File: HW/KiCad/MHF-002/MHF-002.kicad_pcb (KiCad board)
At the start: 4 copper layers, 100 x 100 mm, 305 parts, among them J1 VGA, J10 I2C, J100 x, J101 x, J102 x, J103 x, J104 x, J105 x, J106 x, J107 +3V3, J108 GND, J109 +3V3, J11 + 5V -, J110 +5V, J111 GND, J112 GND, J113 SDCard, J114 VIN, J115 VI, J116 GND, J12 Reset, J13 +5V, J14 GND, J15 AREF, J16 XTAL2, J17 SDcard, J18 XTAL1, J19 AVCC, J2 PS/2, J21 x, J22 x, J23 VIN 12V, J24 AND_B1, J25 AND_B2, J26 AND_C1, J27 AND_C2, J28 AND_D1, J29 AND_D2, J3 RCA, J30 AND_Dx, J31 AND_Cx, J32 AND_Bx, J33 NOTF, J34 NOTE, J35 NOTEx, J36 NOTFx, J37 x, J38 x, J39 x, J4 SysBus, J40 x, J41 x, J42 x, J43 x, J44 x, J45 x, J46 x, J47 x, J48 x, J49 x, J5 Micro, J50 x, J51 x, J52 x, J53 x, J54 x, J55 x, J56 x, J57 x, J58 x, J59 x, J6 SysBus, J60 x, J61 x, J62 x, J63 x, J64 x, J65 x, J66 x, J67 x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

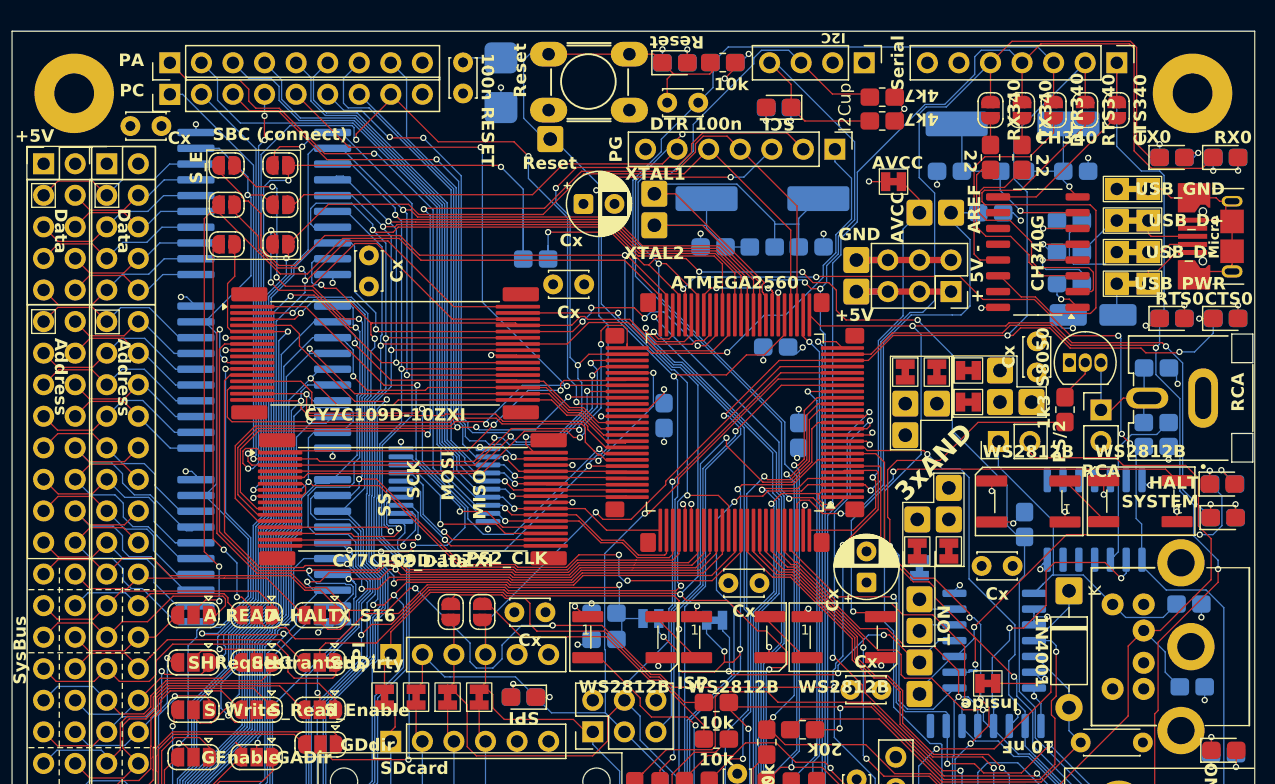
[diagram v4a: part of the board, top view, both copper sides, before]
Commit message: 3xAND routed
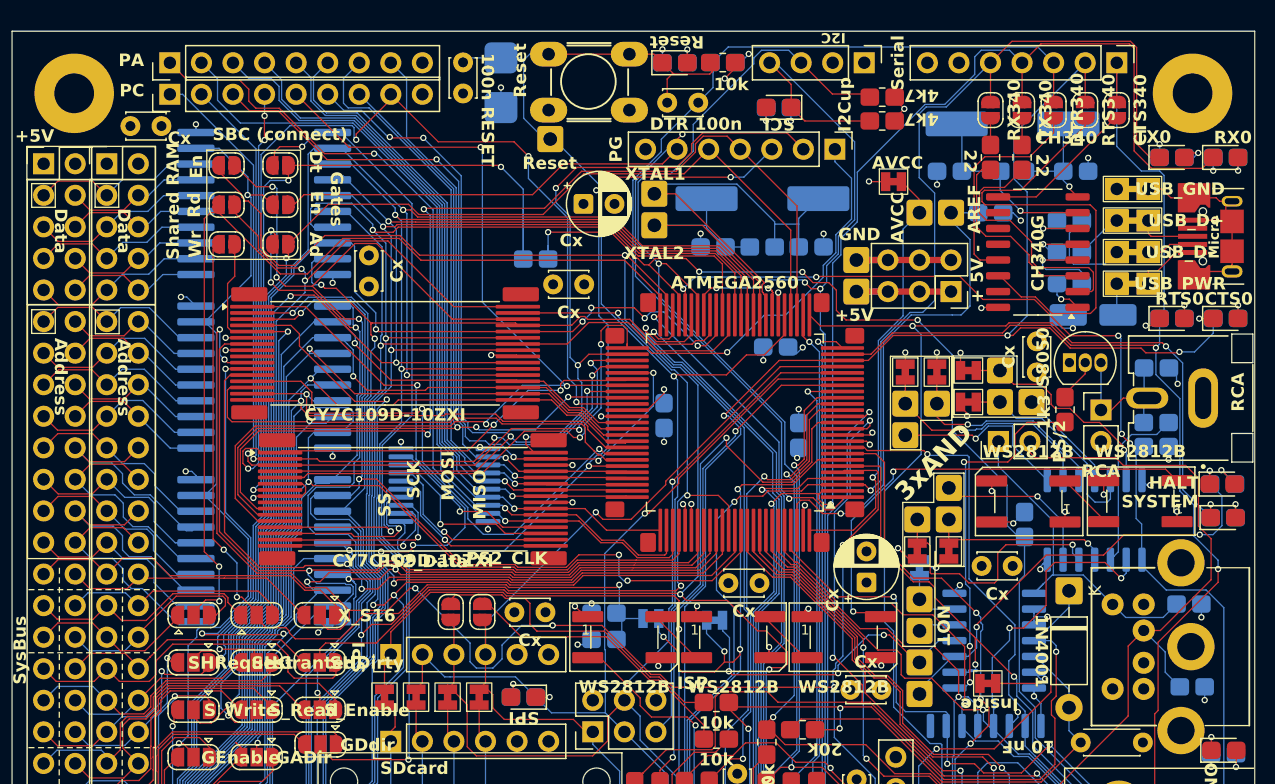
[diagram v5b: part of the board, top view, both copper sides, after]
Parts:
- turned JP94 to 0 degrees
- turned JP95 to 0 degrees
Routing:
- net Net-(J25-Pin_1): track 0.00 -> 21.0 mm, vias 0 -> 1
- net Net-(J26-Pin_1): track 0.00 -> 18.8 mm, vias 0 -> 1
- net Net-(J29-Pin_1): track 0.06 -> 17.7 mm, vias 0 -> 1
- net Net-(J27-Pin_1): track 0.00 -> 17.4 mm, vias 0 -> 1
- net Net-(J28-Pin_1): track 0.00 -> 17.2 mm
- net Net-(J24-Pin_1): track 0.00 -> 14.9 mm, vias 0 -> 1
- net Net-(J31-Pin_1): track 0.00 -> 14.7 mm, vias 0 -> 1
- net Net-(J32-Pin_1): track 0.00 -> 13.4 mm, vias 0 -> 1
- net Net-(R4-Pad1): track 40.7 -> 29.5 mm, vias 1 -> 3
- net +5V: track 92.0 -> 101.6 mm, vias 49 -> 55
- net Net-(J30-Pin_1): track 0.00 -> 8.39 mm
- net B_READ: track 9.87 -> 16.7 mm
- net A_READ: track 19.2 -> 13.5 mm
- net B_HALT: track 15.5 -> 18.5 mm
- net A_HALT: track 21.1 -> 19.1 mm
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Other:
- board text added: "Ad"
- board text added: "Dt"
- board text added: "En"
- board text added: "Gates"
- board text added: "Rd"
- board text added: "Shared RAM"
- board text added: "Wr"
- board text removed: "S_E"
